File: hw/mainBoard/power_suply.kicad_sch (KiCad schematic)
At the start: 29 parts, among them Q1 NMOS, Q2 NMOS, U4 LM5148RGYR

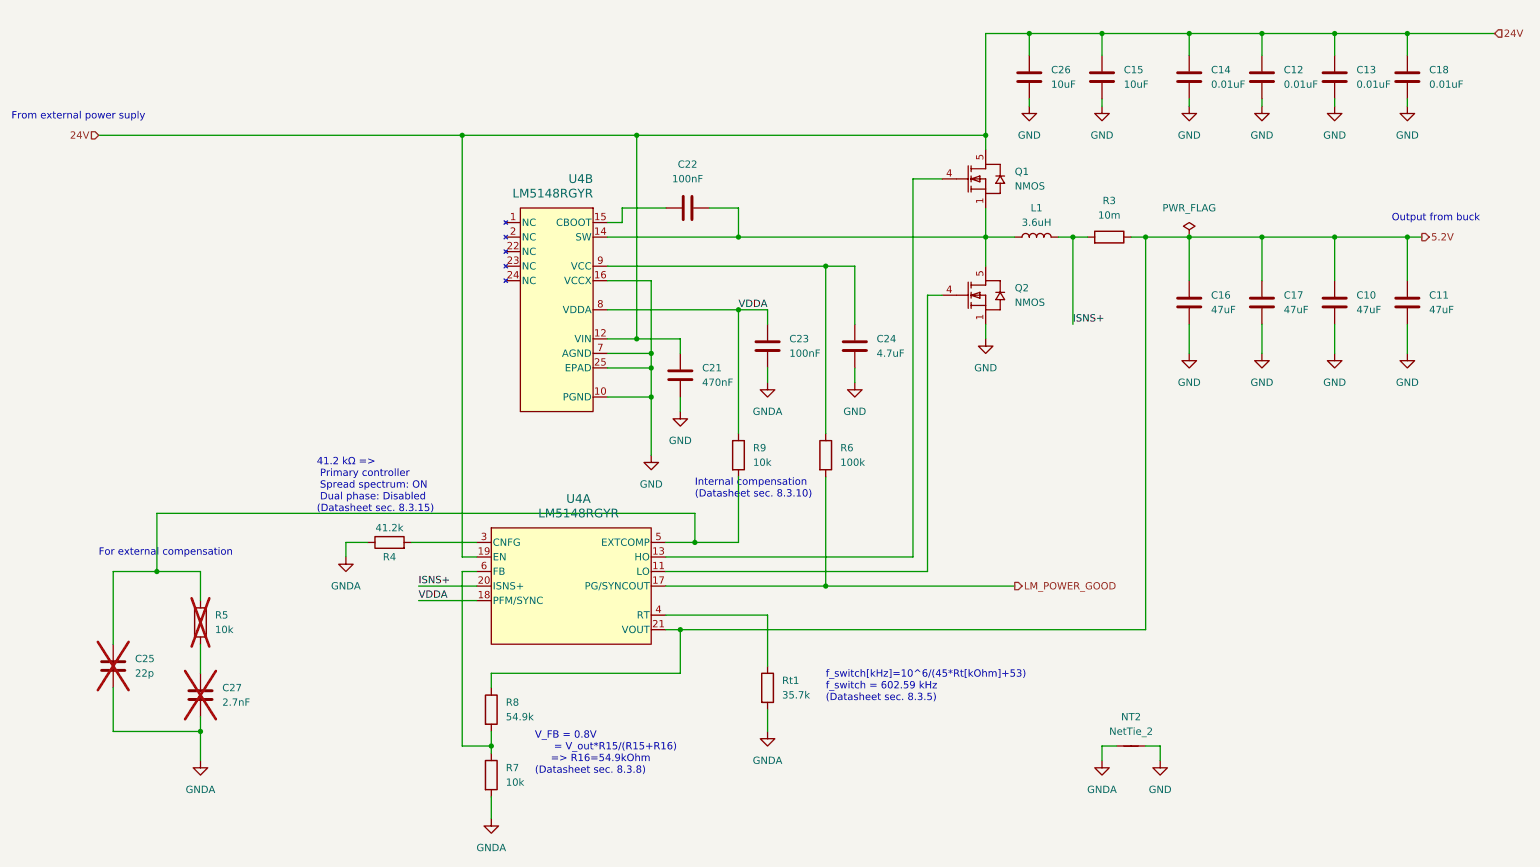
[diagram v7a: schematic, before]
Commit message: text - periferie, obrazky hw - schemata
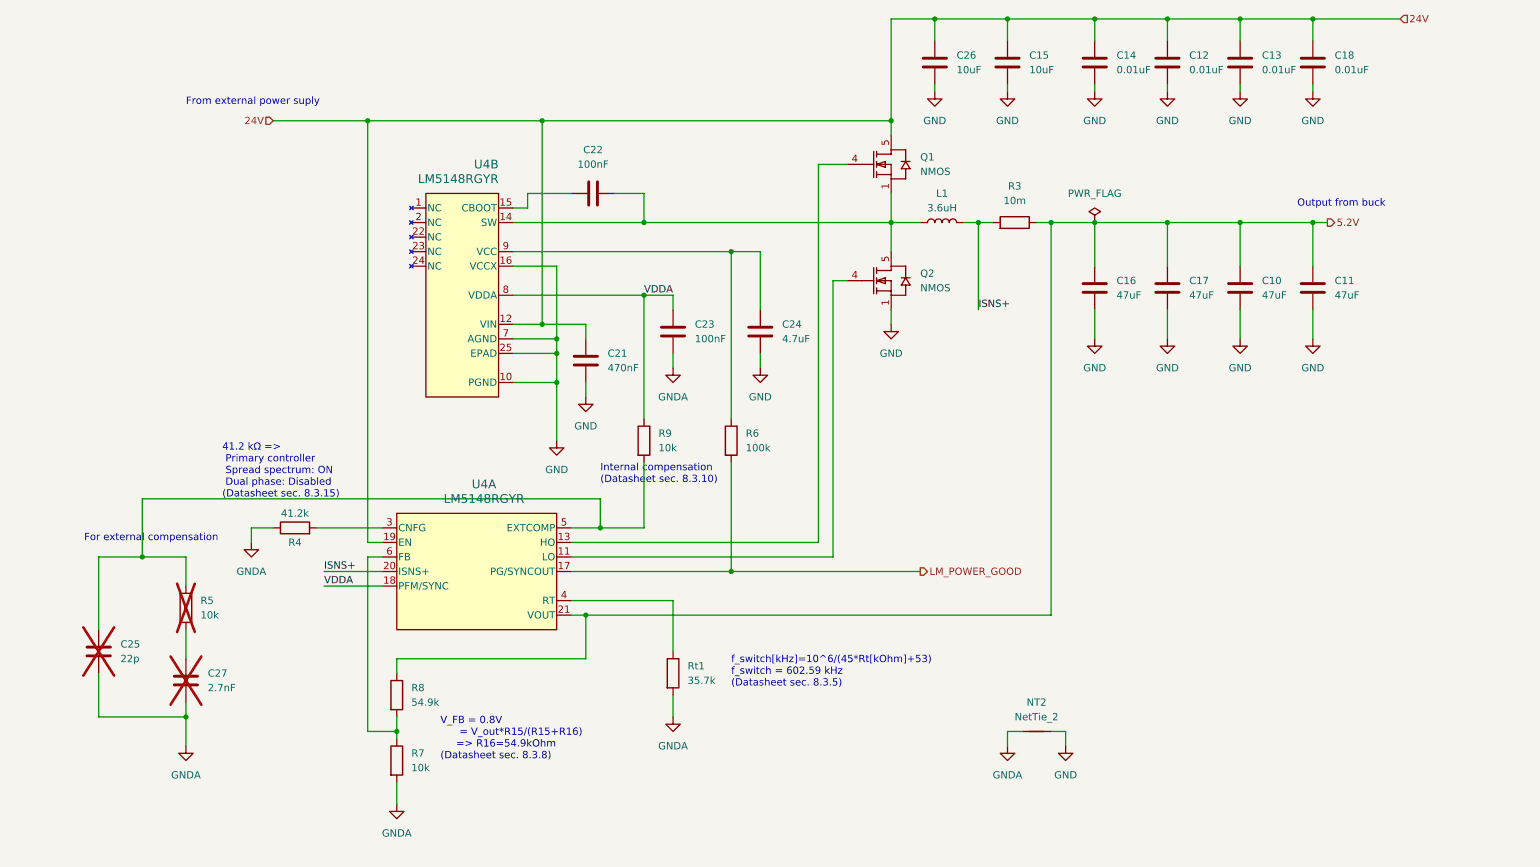
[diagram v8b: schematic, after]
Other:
- moved on the sheet: C10, C11, C12, C13, C14, C15, C16, C17, C18, C21, C22, C23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
